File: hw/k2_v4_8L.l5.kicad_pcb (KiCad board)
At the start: 8 copper layers, 120 x 46 mm, 59 parts, among them J11 J_EC_HEADER, J12 J_12V_IN, J13 J_SWD, J2 SlimSAS_x8_SFF8654, J3 MCIO_4i_SFF1016, J4 MCIO_4i_SFF1016, J6 J_PWR_CTRL, J9 J_OOB_HEADER, U1 STM32G0B1CBT6, U2 DCDC_12V_3V3, U4 BAT54C, U5 OPTO_LTV356T, U6 DS320PR1601

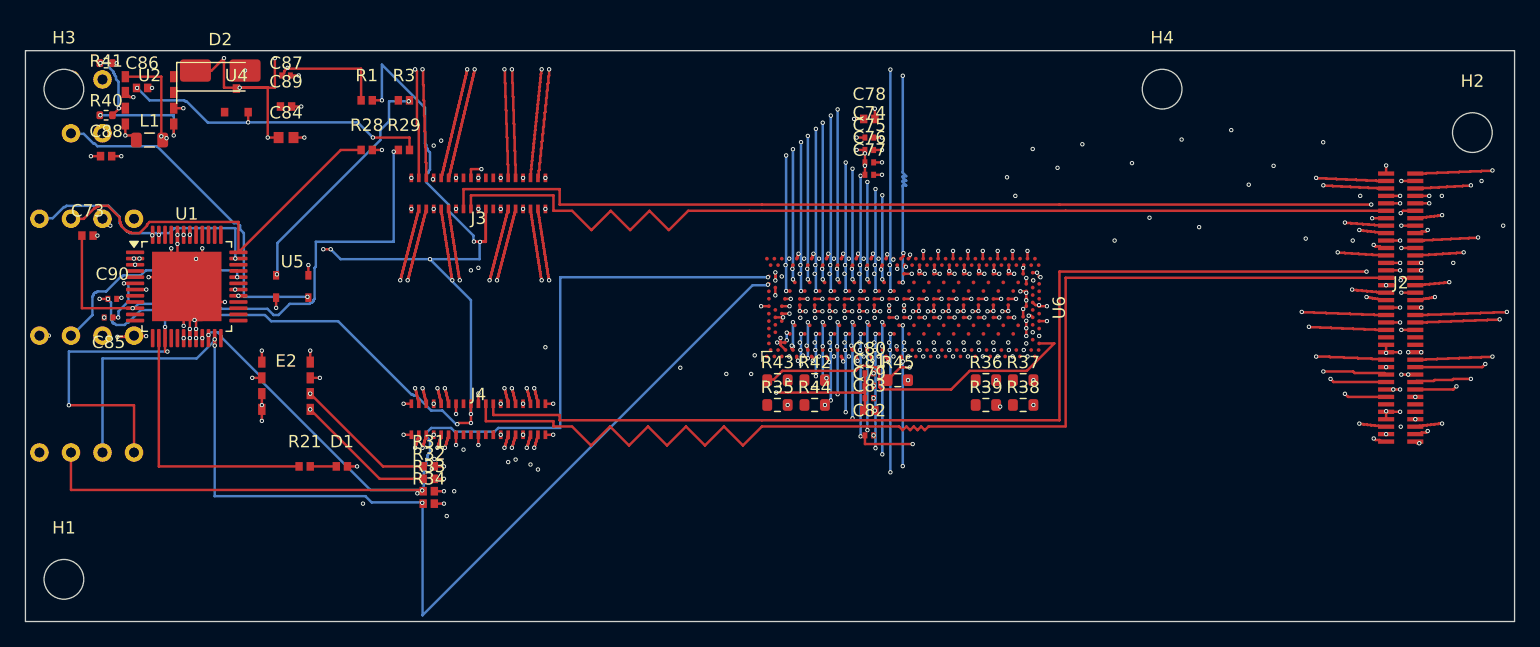
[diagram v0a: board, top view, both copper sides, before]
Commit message: p4(k2): 增量 15（L2 自裁，低速/边带/strap 长逃逸布线）—— 新器 k2_p4_mroute_v1.py 未连接 15->3、门禁违规集零新增、复跑逐字节同 + T-29..T-33
- 依据 owner #14（L2 = 走廊/布线/过孔策略 = 自裁勿停）+ 监理 #K2-19 §二（授权新写确定性执行器）；
  唯一 owner 硬闸 §5-5 H3（连带 12V_IN）未动。
- 既有工具链复跑（现板）：F1 只解 1 条（PERSTA# U1.11<->U1.12 同网相邻盘 0.5mm）；F2/F3/G 对残边全 0 解
  => 根因 T-29：F3 搜索窗 = 两端 bbox +-1mm，而真实走廊（南侧 y 68..78 B.Cu 围裙 / In5 高速道）在窗外。
- 新执行器 k2/tools/k2_p4_mroute_v1.py：多层 A*(F/In2/In5/B) + 只用板内既有 5 个 span 孔类 + 窗扩 14mm
  + 粗搜 0.25/精搜 0.10 + 栅格余量逐级重试 + 精确放行闸（层感知 seg_exact / span 感知 via_exact）
  + 落板后区域重填 + T-22 守卫；纯增、0/45/90、单腿 >=0.05、uuid5 派生、幂等。
- 施工：11 条边解出（PERSTA#x2 / PERSTB# / I2C1_SCL / I2C1_SDA / PWR_BTN_OUT / strap x5）
  = 502 段 + 38 孔 / 549.5383mm；板 k2_v4_8L.l5.kicad_pcb = f8eeeda2495fb891（pro 未变 f68a5fb2f82bd02d）。
- 实测（仓库口径 T-8）：违规 51->51（逐条签名新增 0 / 消失 0）、未连接 15->3、非45 0/4250->0/4753、
  对内等长 max 0.0788 不变、段 4250->4753、孔 674->712、总长 5681.1056->6231.1438；判定器 PASS6/FAIL4 集合未变；
  两次独立复跑逐字节同。
- T-30 孔 oracle 四配对 max（首版漏 hole_clearance 2 条已修）；T-31 栅格剪枝不得清格；T-32 U6 仅外缘逃逸；
  T-33 strap 组走廊容量 5/7（三种顺序均 11/15）。
- 残余 3（fail-closed）：12V_IN（H3 硬闸）/ DS320_STRAP_A_ADDR0_15-8（R42.1 端点局部不可解）/
  DS320_STRAP_MODE（strap 组走廊容量）。
- SPEC 留痕 rev-43 = a98e3c482cdc15af（_spec_rev_33 卡，叶级 diff = spec_version + 22 新叶、删除 0；
  rev-19..42 原件逐字节未动）+ project.yaml 重指向；W-7 九条 ignore 逐条方案草案（含机读复算 pre/post）
  交监理逐条批。未改生成器/原理图/判据；未放松任何 DRC 下限。
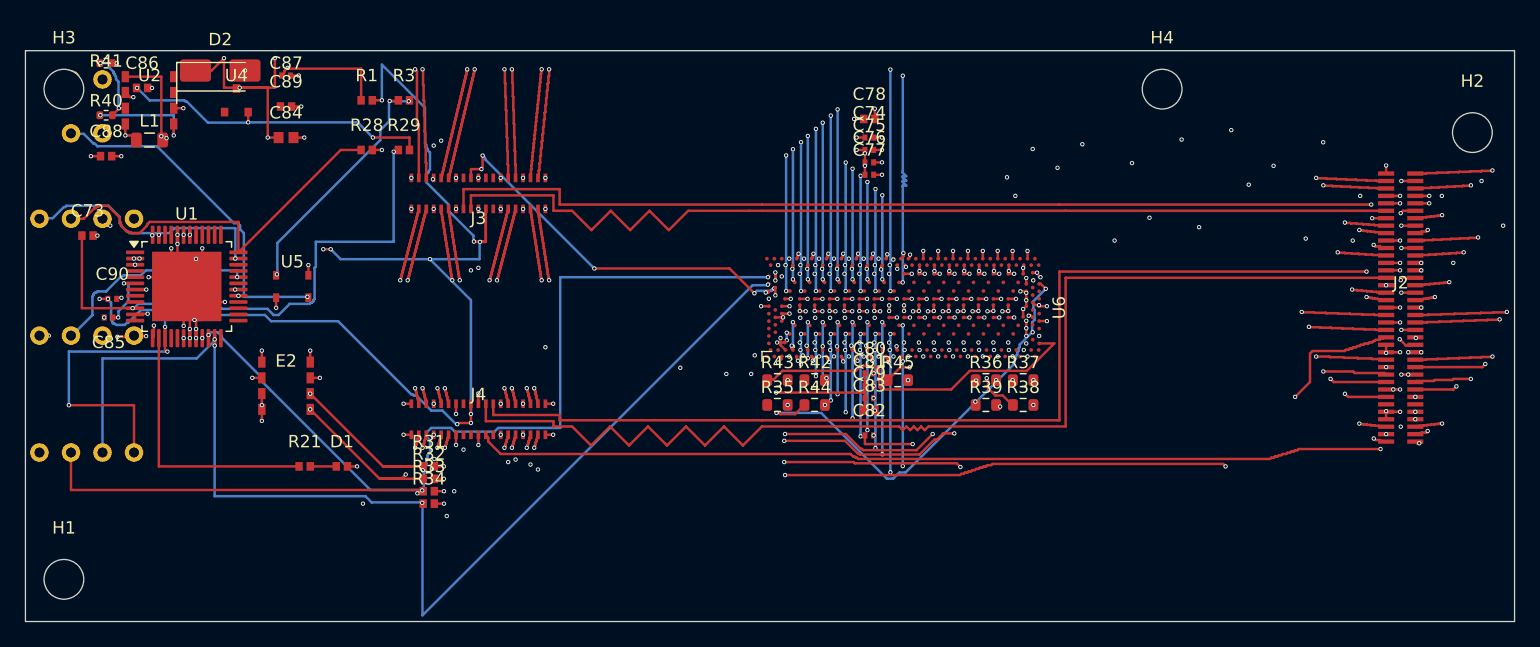
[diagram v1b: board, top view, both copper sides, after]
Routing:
- net PERSTA#: track 51.5 -> 152.3 mm, vias 2 -> 9
- net I2C1_SDA: track 43.1 -> 135.3 mm, vias 2 -> 7
- net I2C1_SCL: track 34.7 -> 122.0 mm, vias 2 -> 6
- net PERSTB#: track 0.00 -> 77.9 mm, vias 0 -> 2
- net DS320_STRAP_B_ADDR1_7-0: track 0.00 -> 38.0 mm, vias 0 -> 2
- net DS320_STRAP_B_ADDR0_15-8: track 0.00 -> 35.7 mm, vias 0 -> 2
- net DS320_STRAP_B_ADDR0_7-0: track 0.00 -> 30.3 mm, vias 0 -> 5
- net DS320_STRAP_A_ADDR0_7-0: track 0.00 -> 30.2 mm, vias 0 -> 4
- net PWR_BTN_OUT: track 0.00 -> 29.2 mm, vias 0 -> 3
- net DS320_STRAP_A_ADDR1_7-0: track 0.00 -> 28.5 mm, vias 0 -> 4

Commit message: p4(k2): 增量 16（L2 自裁，M15 阶段重做）—— 确定性优先序（strap 组优先）⇒ 未连接 3->2；器内禁同格连续换层（堆叠孔 = holes_co_located 门禁）+ 自孔两两判定
- 依据：监理本轮续推（P4 内继续 L2 收敛，不越阶段）+ owner #14（L2 = 走廊/布线/过孔策略 = 自裁勿停）。
- 动因（T-36）：增量 15 后残 3 中两条 strap 均为**东缘球**（U6.FF5 / U6.FF24）且只能球心盘中孔逃逸；
  R35..R44 行南向 F.Cu 出口唯一（x≈80.5..82.3），南墙 = PCIE_REFCLK1_P/N 长度匹配对（对内等长 0.0）⇒ 不可挪
  ⇒ 性质是走廊容量/分配，不是搜索不足。
- T-34：**处理顺序即分配手段** —— 同器同板仅改确定性优先序（--order list + PRIORITY_NETS = strap 组 7 条固定序 -> 其余 dist_asc），
  解数 11 -> 12（6 条可行 strap 全落 + 侧带 4 + PERSTA# 2）；三种非优先序均停在 11 且失败集轮换。
- T-35：允许「同格连续换层」会形成同点两孔 => KiCad holes_co_located（非 ignore 族 = 门禁），首版实测 +1；
  修法 = 器内禁止同格连续换层（viaf 守卫）+ 本路由自身孔间两两判定（孔-孔/孔-铜，同网无豁免）=> 修正后新增 0。
- 施工：M15 重做（450 段/39 孔/591.6814mm，取代增量 15 的 502/38/549.5383）；板 = d9813bc554a2d611（pro 未变 f68a5fb2f82bd02d）。
- 实测（仓库口径 T-8）：违规 51->51（逐条签名对增量 15 前基线新增 0/消失 0）、未连接 3->2、非45 0/4701、
  对内等长 max 0.0788 不变、段 4753->4701、孔 712->713、总长 6231.1438->6273.2870；判定器 PASS6/FAIL4 集合未变；
  两次独立复跑逐字节同。
- W-7 九条复算：8 项零变化；track_not_centered_on_via 28->30（与增量 15 同 2 条，本增量未再增）。
- 残余 2（fail-closed）：12V_IN（owner 硬闸 §5-5 H3）/ DS320_STRAP_A_ADDR0_15-8（R42.1 端点局部不可解，±1.2mm 内 5 span 类
  全无合法孔位，F.Cu 逃逸域 24 格）=> 放置/既有铜级处置，超 ENG 自裁域。
- SPEC 留痕 rev-44 = acc64b447ef55e90（_spec_rev_34 卡，叶级 diff = spec_version + 22 新叶、删除 0；rev-19..43 原件逐字节未动）
  + project.yaml 重指向；状态件 v18（§25）。未改生成器/原理图/判据；未放松任何 DRC 下限。
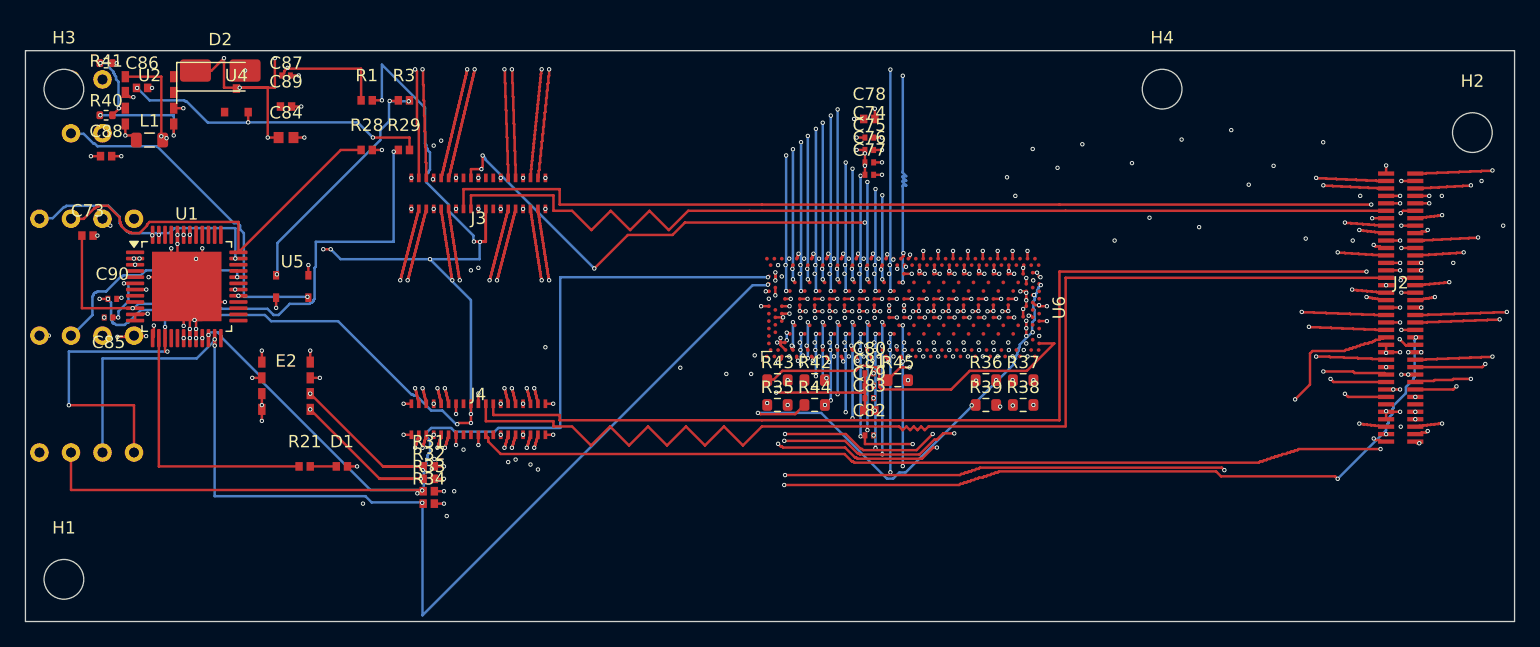
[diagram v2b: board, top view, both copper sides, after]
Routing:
- net DS320_STRAP_MODE: track 0.00 -> 37.4 mm, vias 0 -> 3
- net DS320_STRAP_B_ADDR1_7-0: track 38.0 -> 34.9 mm, vias 2 -> 4
- net DS320_STRAP_B_ADDR0_7-0: track 30.3 -> 33.4 mm, vias 5 -> 3
- net DS320_STRAP_B_ADDR0_15-8: track 35.7 -> 38.3 mm
- net PERSTA#: track 152.3 -> 154.3 mm, vias 9 -> 8
- net I2C1_SDA: track 135.3 -> 135.2 mm, vias 7 -> 6

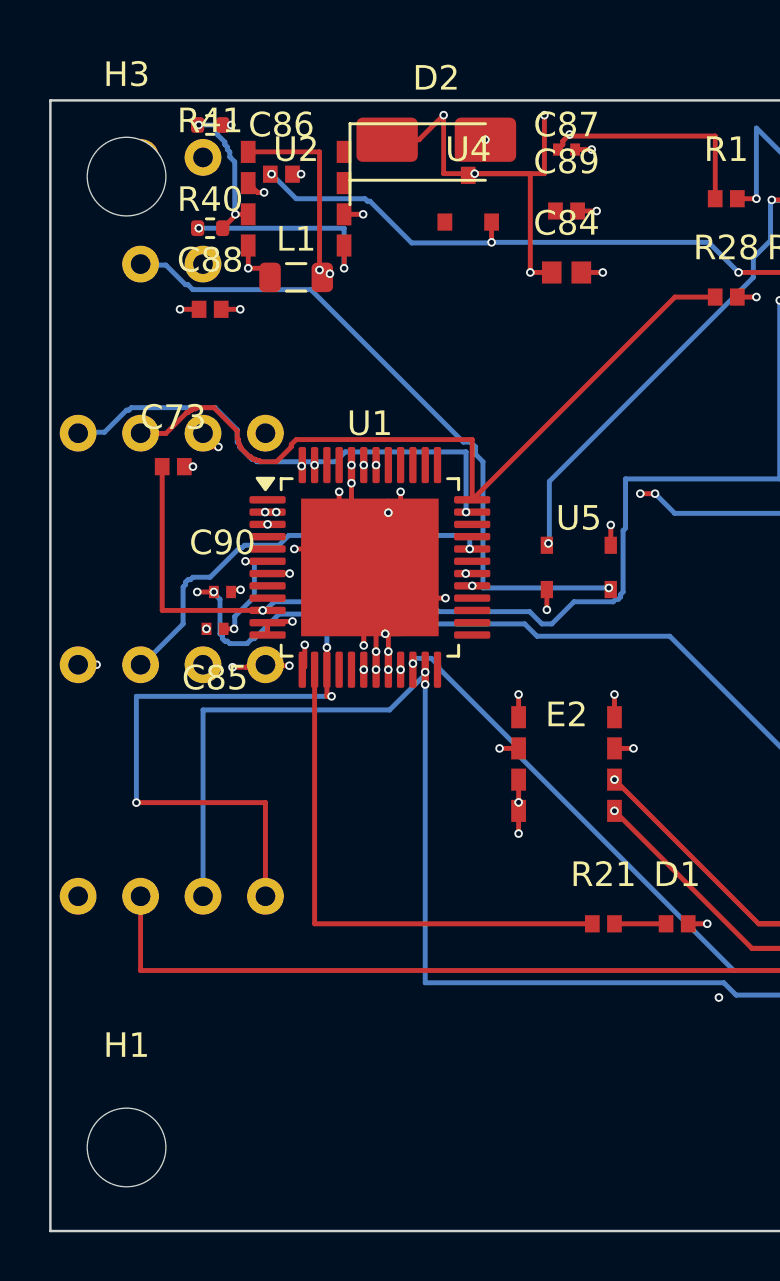
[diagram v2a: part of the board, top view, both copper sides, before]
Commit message: p4(k2): H3 重解 4 孔（L2 热机械，监理 #K2-19 §一-3）→ (45.1,75.1) + 12V_IN In4 面延伸接入 J12.1；SPEC rev-45
- H3(26.1,36.1) 与 J12/J6 排针列（column_x=27.94, P3-4 冻结）硬冲突；左缘 Ø6.0 净空不可得 ⇒ 按裁重解孔位（不降孔数/不缩 keepout/不移排针列）
- 4 孔实测（边料/Ø6.0净空 t-v/pad, mm）：H1 1.50/7.123/5.764 · H2 1.80/3.019/5.037 · H3 2.30/6.100/8.250 · H4 1.50/4.178/18.079 ⇒ 全满足（含 pad）
- 新增同网 In4 12V_IN zone（PDN，L2）+ ZONE_FILLER 重填（T-25）；未动任何 segment/via
- 实测：DRC error 15→0（违规 51→35，余 = lib_footprint_mismatch 35，按 W-8 以板为准 disposition）；未连接 2→1；非45 0/4701；段/孔/总长 4701/713/6273.2870 逐字节同；对内等长 max 0.0788 不变；判定器 PASS6/FAIL4 集合未变
- 板 sha d9813bc5→accc7168d4a247bc；pro f68a5fb2f82bd02d 未变；zone 17→18（铜区 9→10，登记供监理）
- SPEC：新增 rev-45 留痕（_spec_rev_35），spec_name→rev-45；rev-19..44 原件逐字节未动
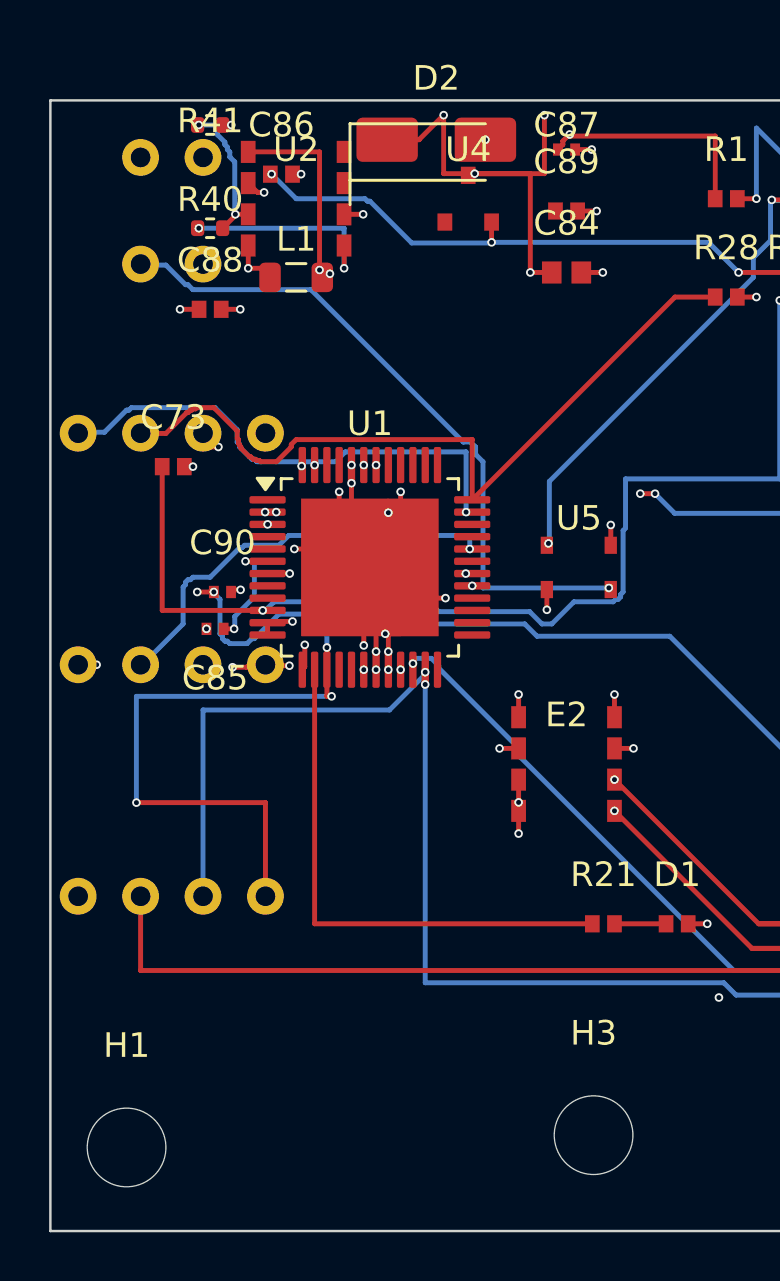
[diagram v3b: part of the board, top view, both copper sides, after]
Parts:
- moved H3 43.4 mm to (45.1, 75.1)
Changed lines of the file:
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@@
 	(footprint "MountingHole_3.2mm_M3"
 		(layer "F.Cu")
-		(at 26.1 36.1)
+		(at 45.1 75.1)
 		(descr "Mounting Hole 3.2mm, M3, no annular, generated by kicad-footprint-generator mountinghole.py")
 		(tags "mountinghole M3")
@@
 		(polygon
 			(pts
-				(xy 29.1 36.1) (xy 29.054423 36.620944) (xy 28.919077 37.12606) (xy 28.698076 37.6) (xy 28.398133 38.028362)
-				(xy 28.028362 38.398133) (xy 27.6 38.698076) (xy 27.12606 38.919077) (xy 26.620944 39.054423) (xy 26.1 39.1)
-				(xy 25.579055 39.054423) (xy 25.073939 38.919077) (xy 24.6 38.698076) (xy 24.171637 38.398133) (xy 23.801866 38.028362)
-				(xy 23.501923 37.6) (xy 23.280922 37.12606) (xy 23.145576 36.620944) (xy 23.1 36.1) (xy 23.145576 35.579055)
-				(xy 23.280922 35.073939) (xy 23.501923 34.6) (xy 23.801866 34.171637) (xy 24.171637 33.801866) (xy 24.6 33.501923)
-				(xy 25.073939 33.280922) (xy 25.579055 33.145576) (xy 26.1 33.1) (xy 26.620944 33.145576) (xy 27.12606 33.280922)
-				(xy 27.6 33.501923) (xy 28.028362 33.801866) (xy 28.398133 34.171637) (xy 28.698076 34.6) (xy 28.919077 35.073939)
-				(xy 29.054423 35.579055)
+				(xy 48.1 75.1) (xy 48.054423 75.620944) (xy 47.919077 76.12606) (xy 47.698076 76.6) (xy 47.398133 77.028362)
+				(xy 47.028362 77.398133) (xy 46.6 77.698076) (xy 46.12606 77.919077) (xy 45.620944 78.054423) (xy 45.1 78.1)
+				(xy 44.579055 78.054423) (xy 44.073939 77.919077) (xy 43.6 77.698076) (xy 43.171637 77.398133) (xy 42.801866 77.028362)
+				(xy 42.501923 76.6) (xy 42.280922 76.12606) (xy 42.145576 75.620944) (xy 42.1 75.1) (xy 42.145576 74.579055)
+				(xy 42.280922 74.073939) (xy 42.501923 73.6) (xy 42.801866 73.171637) (xy 43.171637 72.801866) (xy 43.6 72.501923)
+				(xy 44.073939 72.280922) (xy 44.579055 72.145576) (xy 45.1 72.1) (xy 45.620944 72.145576) (xy 46.12606 72.280922)
+				(xy 46.6 72.501923) (xy 47.028362 72.801866) (xy 47.398133 73.171637) (xy 47.698076 73.6) (xy 47.919077 74.073939)
+				(xy 48.054423 74.579055)
 			)
 		)
@@
 			)
 		)
+	)
+	(zone
+		(net "12V_IN")
+		(layer "In4.Cu")
+		(hatch edge 0.5)
+		(priority 2)
+		(connect_pads yes
+			(clearance 0.2)
+		)
+		(min_thickness 0.25)
+		(fill yes
+			(thermal_gap 0.2)
+			(thermal_bridge_width 0.3)
+			(island_removal_mode 0)
+		)
+		(polygon
+			(pts
+				(xy 24.6 34.9) (xy 29.4 34.9) (xy 29.4 41.2) (xy 24.6 41.2)
+			)
+		)

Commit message: p4(k2): strap DS320_STRAP_A_ADDR0_15-8 走廊/placement 重解（L2 自裁，#K2-20 §三）；SPEC rev-46
- 根因实测：R42.1(85.775,59.55) F.Cu 可达域 = 封闭口袋 x[85.0,86.75]·y[59.15,60.15]；0.01mm 全域扫描 0 个合法孔位（F→In2/In5/B 全 0）；阻断 = R42.1 盘下 In2 PCIE_DN1_P（SMD 盘对 In2 不可见族）
- 施工（纯增，T-22/T-25，幂等执行器）：R42 (86.6,59.55)→(93.3,61.55)（SPEC strap_domain zone 内 row2 空槽，位移 6.99mm）+ F.Cu 2 段 + In2.Cu 2 段 + F→In2 盲孔 + U6.FF5 盘中孔 + 原 GND 盘中孔随搬；ZONE_FILLER 重填
- 复跑：未连接 1→0；违规 35→35（error 0，集合未变零新增）；非45 0/4705；段/孔/长 4705/715/6287.3747（+14.0877mm）；对内等长 0.0788 不变；冻结判定器 PASS6/FAIL4 同；草案 PASS12/FAIL6→PASS13/FAIL5
- 板 accc7168d4a247bc→37019705ef994ccc；pro f68a5fb2f82bd02d 未变；冻结四源+配套+rev-19..45 原件逐字节未动
- SPEC rev-46 = rev-45 + _spec_rev_36 留痕（spec_version bump；project.yaml spec_name 同步）
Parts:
- moved R42 6.99 mm to (93.3, 61.5)
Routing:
- net DS320_STRAP_A_ADDR0_15-8: track 0.00 -> 14.1 mm, vias 0 -> 2
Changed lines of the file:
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@@
 	(footprint "R_0603_1608Metric"
 		(layer "F.Cu")
-		(at 86.6 59.55)
+		(at 93.3 61.55)
 		(descr "Resistor SMD 0603 (1608 Metric), square (rectangular) end terminal, IPC-7351 nominal, (Body size source: IPC-SM-782 page 72, https://www.pcb-3d.com/wordpress/wp-content/uploads/ipc-sm-782a_amendment_1_and_2.pdf)")
 		(tags "resistor")
@@
 	)
 	(via blind
-		(at 87.5468 59.3913)
+		(at 94.025 61.55)
 		(size 0.35)
 		(drill 0.2)
@@
 	)
 	(segment
+		(start 92.475 61.55)
+		(end 93.275 60.75)
+		(width 0.2)
+		(layer "F.Cu")
+		(net "DS320_STRAP_A_ADDR0_15-8")
+	)
+	(segment
+		(start 93.275 60.75)
+		(end 100.075 60.75)
+		(width 0.2)
+		(layer "F.Cu")
+		(net "DS320_STRAP_A_ADDR0_15-8")
+	)
+	(via blind
+		(at 104.1704 56.29)
+		(size 0.35)
+		(drill 0.2)
+		(layers "F.Cu" "In2.Cu")
+		(net "DS320_STRAP_A_ADDR0_15-8")
+	)
+	(via blind
+		(at 100.075 60.75)
+		(size 0.35)
+		(drill 0.2)
+		(layers "F.Cu" "In2.Cu")
+		(net "DS320_STRAP_A_ADDR0_15-8")
+	)
+	(segment
+		(start 104.1704 56.6546)
+		(end 104.1704 56.29)
+		(width 0.2)
+		(layer "In2.Cu")
+		(net "DS320_STRAP_A_ADDR0_15-8")
+	)
+	(segment
+		(start 100.075 60.75)
+		(end 104.1704 56.6546)
+		(width 0.2)
+		(layer "In2.Cu")
+		(net "DS320_STRAP_A_ADDR0_15-8")
+	)
+	(segment
